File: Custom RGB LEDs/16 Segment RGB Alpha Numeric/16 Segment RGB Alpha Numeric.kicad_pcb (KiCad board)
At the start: 4 copper layers, 101 x 22.9 mm, 209 parts

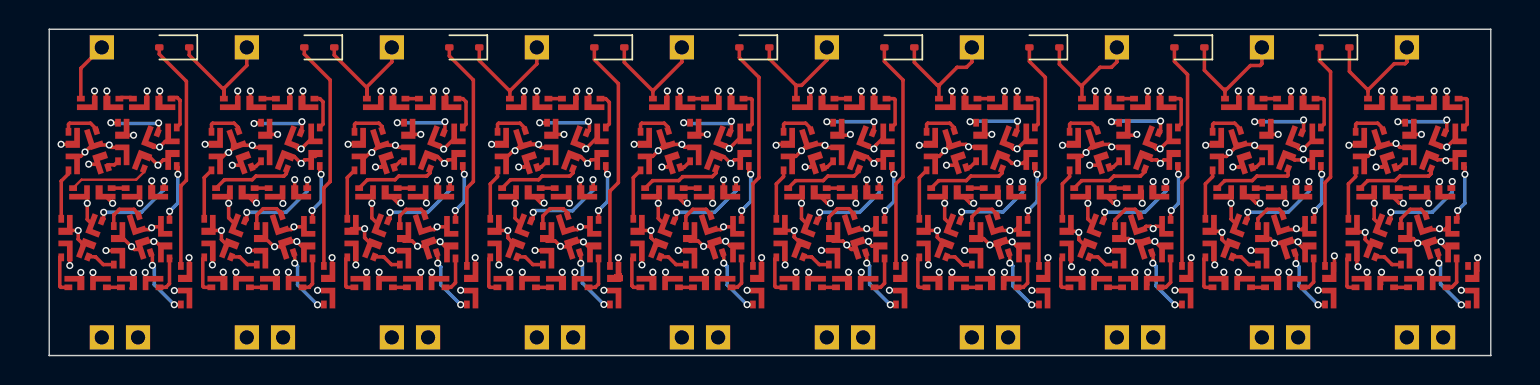
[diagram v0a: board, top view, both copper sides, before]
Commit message: Season 1/2 Speedo board updates
Season 1/2 Speedo board mostly complete, a few modifications still pending.
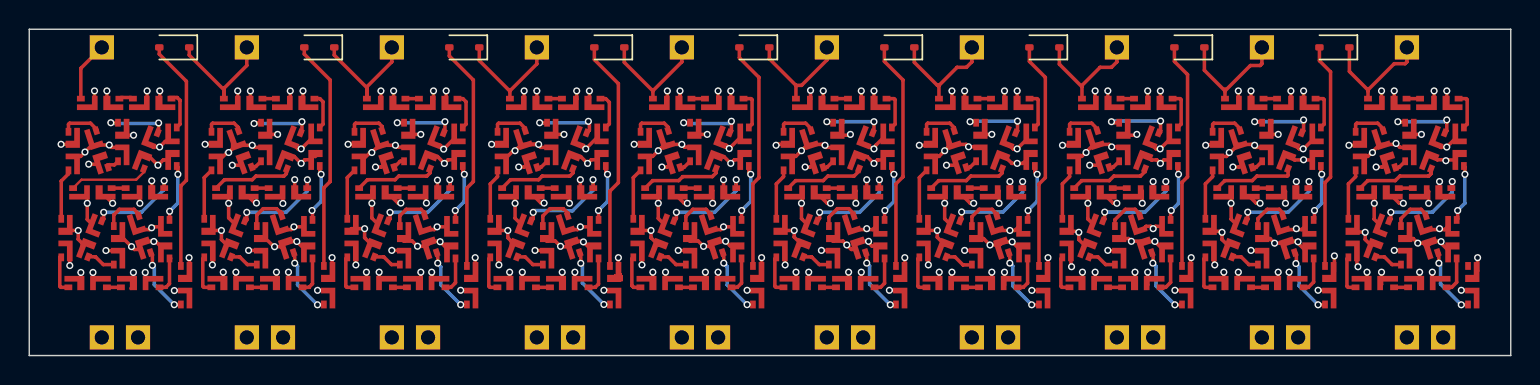
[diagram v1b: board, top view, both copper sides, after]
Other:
- board size 101 x 22.9 mm -> 103.8 x 22.9 mm
